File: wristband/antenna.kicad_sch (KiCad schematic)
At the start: 1 part

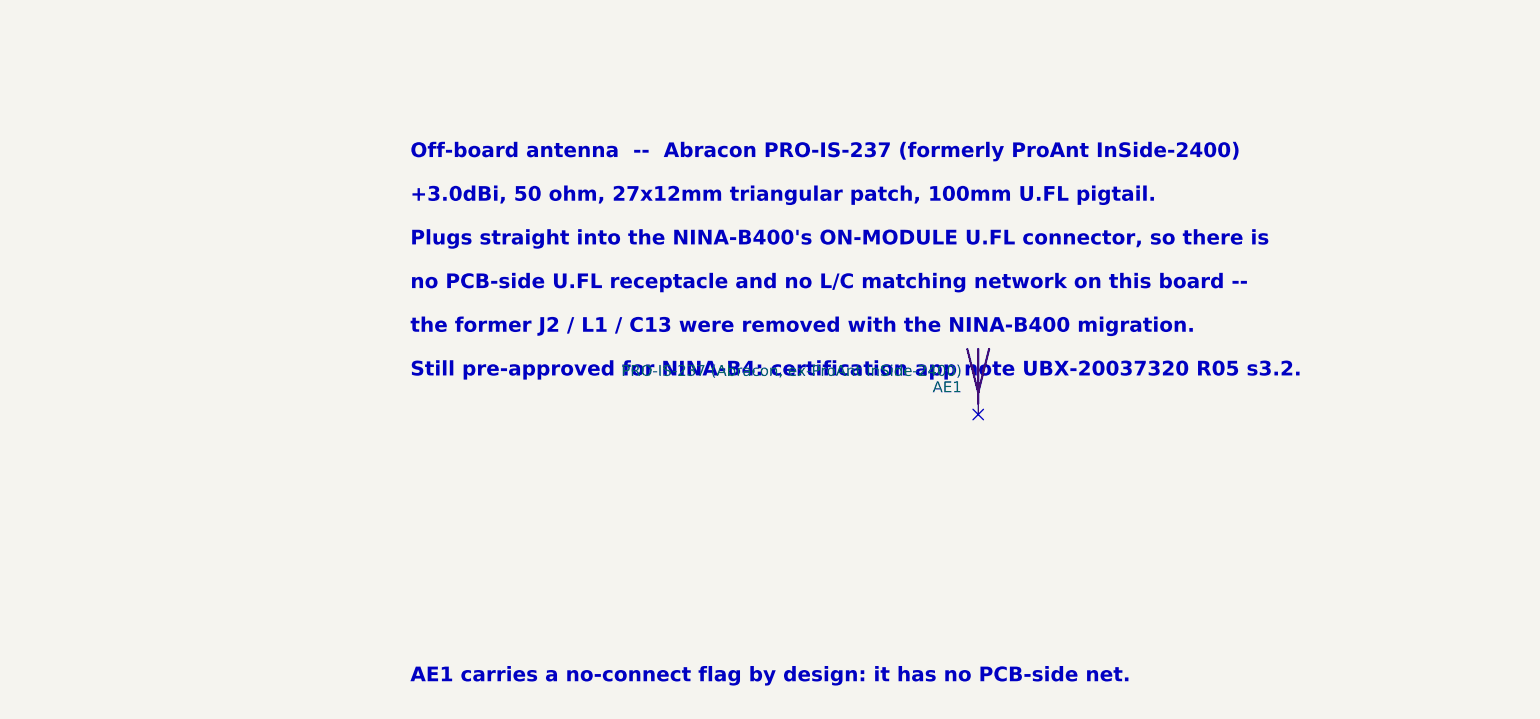
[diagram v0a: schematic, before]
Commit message: Convert global labels to power symbols; import footprints to PCB
Continues the ground cleanup from 0263e7f across the rest of the wristband
sheets: global labels replaced with explicit power symbols and wired
junctions, so connections are drawn rather than implied by name.

                     wires      labels      junctions   symbols
  power_bms          61 -> 83   61 -> 51    0 -> 3      25 -> 36
  programming_debug   7 ->  8    7 ->  4    0 -> 1       1 ->  3
  radio_mcu          71 -> 79   64 -> 42    7 -> 17     18 -> 32
  regulation          7 ->  7    7 ->  4    0 -> 0       3 ->  6

The added symbols are all power ports, so the BOM is untouched: still 47
components, 76 nets, 42 no-connects, 35 analyzer findings with 1 error --
identical before and after. The one error is the known DW01A false
positive (U1.6 GND sits on CELL_N by design, per the reference circuit).

Also ran Update PCB from Schematic on the wristband: 0 -> 46 footprints.
Nothing routed yet, no zones, board outline unchanged.

Co-Authored-By: Claude Opus 5 (1M context) <noreply@anthropic.com>
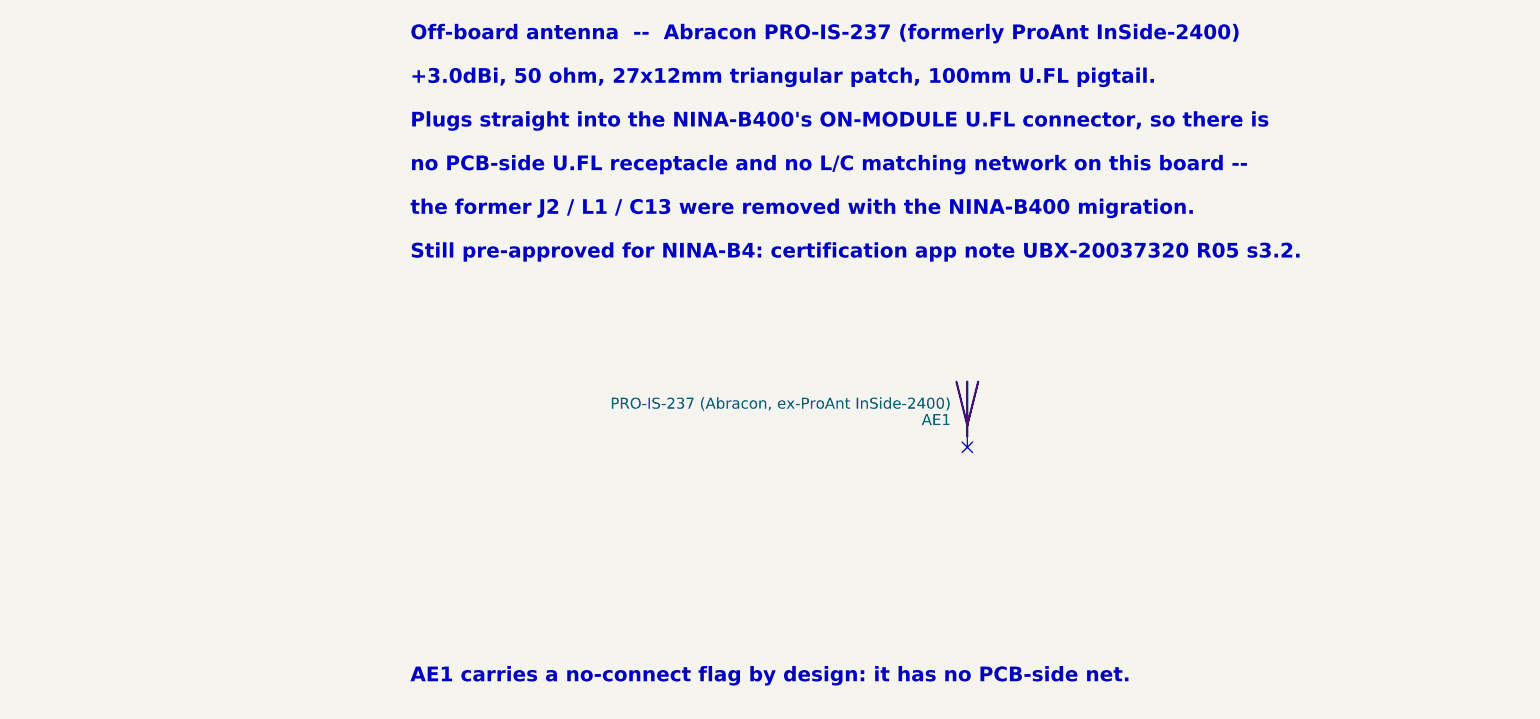
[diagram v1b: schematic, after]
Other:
- moved on the sheet: AE1
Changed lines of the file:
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@@
 	(text "Still pre-approved for NINA-B4: certification app note UBX-20037320 R05 s3.2."
 		(exclude_from_sim no)
-		(at 76.2 76.2 0)
+		(at 76.2 62.484 0)
 		(effects
 			(font
@@
 	(text "Off-board antenna  --  Abracon PRO-IS-237 (formerly ProAnt InSide-2400)"
 		(exclude_from_sim no)
-		(at 76.2 50.8 0)
+		(at 76.2 37.084 0)
 		(effects
 			(font
@@
 	(text "no PCB-side U.FL receptacle and no L/C matching network on this board --"
 		(exclude_from_sim no)
-		(at 76.2 66.04 0)
+		(at 76.2 52.324 0)
 		(effects
 			(font
@@
 	(text "+3.0dBi, 50 ohm, 27x12mm triangular patch, 100mm U.FL pigtail."
 		(exclude_from_sim no)
-		(at 76.2 55.88 0)
+		(at 76.2 42.164 0)
 		(effects
 			(font
@@
 	(text "the former J2 / L1 / C13 were removed with the NINA-B400 migration."
 		(exclude_from_sim no)
-		(at 76.2 71.12 0)
+		(at 76.2 57.404 0)
 		(effects
 			(font
@@
 	(text "Plugs straight into the NINA-B400's ON-MODULE U.FL connector, so there is"
 		(exclude_from_sim no)
-		(at 76.2 60.96 0)
+		(at 76.2 47.244 0)
 		(effects
 			(font
@@
 	)
 	(no_connect
-		(at 142.24 81.28)
+		(at 140.97 85.09)
 	)
 	(symbol
 		(lib_id "Device:Antenna")
-		(at 142.24 76.2 0)
+		(at 140.97 80.01 0)
 		(unit 1)
 		(body_style 1)
@@
 		(dnp no)
 		(property "Reference" "AE1"
-			(at 140.335 78.105 0)
+			(at 139.065 81.915 0)
 			(show_name no)
 			(do_not_autoplace no)
@@
 		)
 		(property "Value" "PRO-IS-237 (Abracon, ex-ProAnt InSide-2400)"
-			(at 140.335 76.2 0)
+			(at 139.065 80.01 0)
 			(show_name no)
 			(do_not_autoplace no)
@@
 		)
 		(property "Footprint" ""
-			(at 142.24 76.2 0)
+			(at 140.97 80.01 0)
 			(hide yes)
 			(show_name no)
@@
 		)
 		(property "Datasheet" ""
-			(at 142.24 76.2 0)
+			(at 140.97 80.01 0)
 			(hide yes)
 			(show_name no)
@@
 		)
 		(property "Description" ""
-			(at 142.24 76.2 0)
+			(at 140.97 80.01 0)
 			(show_name no)
 			(do_not_autoplace no)
@@
 		)
 		(property "MPN" "PRO-IS-237"
-			(at 140.335 78.105 0)
+			(at 139.065 81.915 0)
 			(hide yes)
 			(show_name no)
@@
 		)
 		(property "Manufacturer" "Abracon"
-			(at 140.335 78.105 0)
+			(at 139.065 81.915 0)
 			(hide yes)
 			(show_name no)

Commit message: Migrate wristband to DWM3001C; swap LDO to TPS7A02; fix ERC
Replace the NINA-B400 + DWM3000 pair with a single Qorvo DWM3001C, then
replace the MCP1700 LDO with a nanopower TI TPS7A0233. Wristband ERC goes
from 1 error / 13 warnings to 0 errors / 1 warning.

DWM3001C (U4), verified against Qorvo DS Rev B May 2022:
- Integrates DW3110 UWB + nRF52833 BLE MCU + LIS2DH12 + UWB antenna +
  Bluetooth chip antenna + 38.4MHz crystal. Its nRF52833 is now the host,
  so U3 (NINA-B400) is deleted.
- The DW3110<->nRF52833 SPI is internal, so the board-level UWB SPI bus,
  IRQ/RSTn/WAKEUP, the GPIO5/6 SPI-mode straps (R7/R8), the IRQ pulldown
  (R9) and the external LFXO (Y1/C14/C15) are all gone. C8-C10 too.
- AE1 (PRO-IS-237) removed: the module carries both antennas, so
  antenna.kicad_sch is documentation-only and places nothing.
- SWD moved for the first time: SWD_CLK=2, SWD_DIO=3, RESET=47 (P0.18),
  SWO=28 (P1.00). Battery sense moved to P0.02 = AIN0. Both P1.00=SWO and
  P0.02=AIN0 confirmed in nRF52833 PS v1.7 p825-826.
- Symbol + DWM3001C_PLACEHOLDER footprint are wristband-only, in libs/.
  The footprint has TWO unresolved dimensions (side pitch back-derives to
  1.06375mm; bottom pad row width undimensioned and apparently off-centre).
  VERIFY BEFORE FAB.

TPS7A0233PDBVR (U5), verified against TI SBVS277C:
- Iq 1.6uA typ / 4uA max -> 25nA typ / 46nA max; it was the largest single
  standby draw, bigger than the DWM3001C's own 850nA sleep. Board standby
  ~4.3uA -> ~2.7uA. Accuracy +/-1.5% vs +/-2.5%.
- Not a drop-in: SOT-23-5 1=IN 2=GND 3=EN 4=NC 5=OUT. EN ties to VBAT
  because TPS7A02 is disabled when EN floats and the MCU on this rail
  cannot enable its own supply.
- C12 1uF -> 2.2uF for the 0.5uF effective-capacitance stability floor.
- Symbol is self-contained: KiCad ships no TPS7A02, and every TPS7A05
  sibling is extends-based, which kicad-cli cannot load.

ERC fixes:
- Real bug: regulation.kicad_sch had no labels at all, so U5's input and
  C11 sat on an iso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
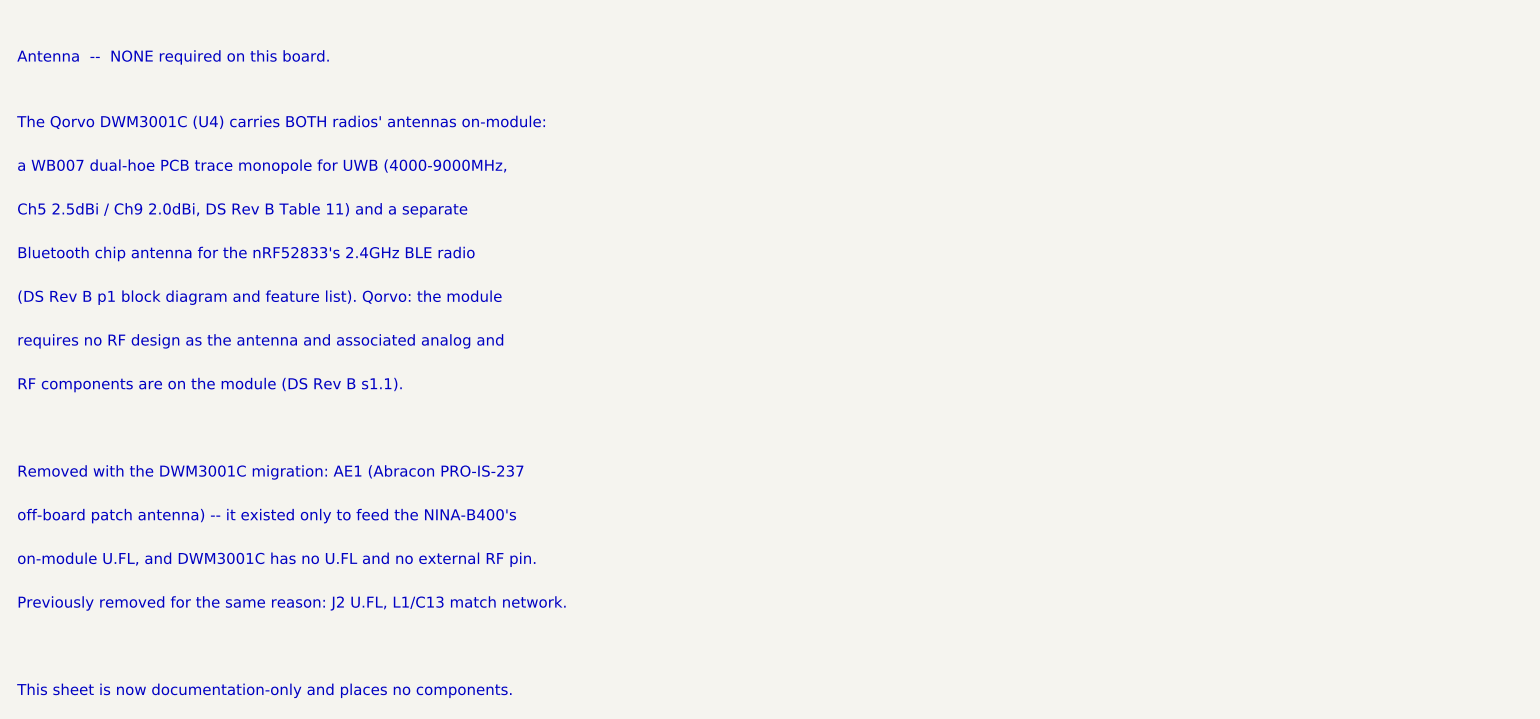
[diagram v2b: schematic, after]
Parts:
- removed AE1: PRO-IS-237 (Abracon, ex-ProAnt InSide-2400), symbol Device:Antenna
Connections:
- no-connect marks 1 -> 0
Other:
- note added: "(DS Rev B p1 block diagram and feature list). Qorvo: the module"
- note added: "Antenna -- NONE required on this board."
- note added: "Bluetooth chip antenna for the nRF52833's 2.4GHz BLE radio"
- note added: "Ch5 2.5dBi / Ch9 2.0dBi, DS Rev B Table 11) and a separate"
- note added: "Previously removed for the same reason: J2 U.FL, L1/C13 match network."
- note added: "RF components are on the module (DS Rev B s1.1)."
- note added: "Removed with the DWM3001C migration: AE1 (Abracon PRO-IS-237"
- note added: "The Qorvo DWM3001C (U4) carries BOTH radios' antennas on-module:"
- note added: "This sheet is now documentation-only and places no components."
- note added: "a WB007 dual-hoe PCB trace monopole for UWB (4000-9000MHz,"
- note added: "off-board patch antenna) -- it existed only to feed the NINA-B400's"
- note added: "on-module U.FL, and DWM3001C has no U.FL and no external RF pin."
- note added: "requires no RF design as the antenna and associated analog and"
- note removed: "+3.0dBi, 50 ohm, 27x12mm triangular patch, 100mm U.FL pigtail."
- note removed: "AE1 carries a no-connect flag by design: it has no PCB-side net."
- note removed: "Off-board antenna -- Abracon PRO-IS-237 (formerly ProAnt InSide-2400)"
- note removed: "Plugs straight into the NINA-B400's ON-MODULE U.FL connector, so there is"
- note removed: "Still pre-approved for NINA-B4: certification app note UBX-20037320 R05 s3.2."
- note removed: "no PCB-side U.FL receptacle and no L/C matching network on this board --"
- note removed: "the former J2 / L1 / C13 were removed with the NINA-B400 migration."
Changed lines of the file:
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@@
 		(comment 1 "Wristband NINA-B400 external antenna -- plugs into the module's ON-BOARD U.FL connector; no PCB-side U.FL or L/C match network needed")
 	)
-	(text "AE1 carries a no-connect flag by design: it has no PCB-side net."
+	(text "Antenna  --  NONE required on this board."
 		(exclude_from_sim no)
-		(at 76.2 111.76 0)
+		(at 30.48 40.64 0)
 		(effects
 			(font
-				(size 1.7 1.7)
-				(bold yes)
+				(size 1.27 1.27)
 			)
-			(justify left)
+			(justify left bottom)
 		)
 	)
-	(text "Still pre-approved for NINA-B4: certification app note UBX-20037320 R05 s3.2."
+	(text "The Qorvo DWM3001C (U4) carries BOTH radios' antennas on-module:"
 		(exclude_from_sim no)
-		(at 76.2 62.484 0)
+		(at 30.48 48.26 0)
 		(effects
 			(font
-				(size 1.7 1.7)
-				(bold yes)
+				(size 1.27 1.27)
 			)
-			(justify left)
+			(justify left bottom)
 		)
 	)
-	(text "Off-board antenna  --  Abracon PRO-IS-237 (formerly ProAnt InSide-2400)"
+	(text "a WB007 dual-hoe PCB trace monopole for UWB (4000-9000MHz,"
 		(exclude_from_sim no)
-		(at 76.2 37.084 0)
+		(at 30.48 53.34 0)
 		(effects
 			(font
-				(size 1.7 1.7)
-				(bold yes)
+				(size 1.27 1.27)
 			)
-			(justify left)
+			(justify left bottom)
 		)
 	)
-	(text "no PCB-side U.FL receptacle and no L/C matching network on this board --"
+	(text "Ch5 2.5dBi / Ch9 2.0dBi, DS Rev B Table 11) and a separate"
 		(exclude_from_sim no)
-		(at 76.2 52.324 0)
+		(at 30.48 58.42 0)
 		(effects
 			(font
-				(size 1.7 1.7)
-				(bold yes)
+				(size 1.27 1.27)
 			)
-			(justify left)
+			(justify left bottom)
 		)
 	)
-	(text "+3.0dBi, 50 ohm, 27x12mm triangular patch, 100mm U.FL pigtail."
+	(text "Bluetooth chip antenna for the nRF52833's 2.4GHz BLE radio"
 		(exclude_from_sim no)
-		(at 76.2 42.164 0)
+		(at 30.48 63.5 0)
 		(effects
 			(font
-				(size 1.7 1.7)
-				(bold yes)
+				(size 1.27 1.27)
 			)
-			(justify left)
+			(justify left bottom)
 		)
 	)
-	(text "the former J2 / L1 / C13 were removed with the NINA-B400 migration."
+	(text "(DS Rev B p1 block diagram and feature list). Qorvo: the module"
 		(exclude_from_sim no)
-		(at 76.2 57.404 0)
+		(at 30.48 68.58 0)
 		(effects
 			(font
-				(size 1.7 1.7)
-				(bold yes)
+				(size 1.27 1.27)
 			)
-			(justify left)
+			(justify left bottom)
 		)
 	)
-	(text "Plugs straight into the NINA-B400's ON-MODULE U.FL connector, so there is"
+	(text "requires no RF design as the antenna and associated analog and"
 		(exclude_from_sim no)
-		(at 76.2 47.244 0)
+		(at 30.48 73.66 0)
 		(effects
 			(font
-				(size 1.7 1.7)
-				(bold yes)
+				(size 1.27 1.27)
 			)
-			(justify left)
+			(justify left bottom)
 		)
 	)
-	(no_connect
-		(at 140.97 85.09)
-	)
-	(symbol
-		(lib_id "Device:Antenna")
-		(at 140.97 80.01 0)
-		(unit 1)
-		(body_style 1)
+	(text "RF components are on the module (DS Rev B s1.1)."
 		(exclude_from_sim no)
-		(in_bom yes)
-		(on_board yes)
-		(in_pos_files yes)
-		(dnp no)
-		(property "Reference" "AE1"
-			(at 139.065 81.915 0)
-			(show_name no)
-			(do_not_autoplace no)
-			(effects
-				(font
-					(size 1.27 1.27)
-				)
-				(justify right)
+		(at 30.48 78.74 0)
+		(effects
+			(font
+				(size 1.27 1.27)
 			)
-		)
-		(property "Value" "PRO-IS-237 (Abracon, ex-ProAnt InSide-2400)"
-			(at 139.065 80.01 0)
-			(show_name no)
-			(do_not_autoplace no)
-			(effects
-				(font
-					(size 1.27 1.27)
-				)
-				(justify right)
-			)
-		)
-		(property "Footprint" ""
-			(at 140.97 80.01 0)
-			(hide yes)
-			(show_name no)
-			(do_not_autoplace no)
-			(effects
-				(font
-					(size 1.27 1.27)
-				)
-			)
-		)
-		(property "Datasheet" ""
-			(at 140.97 80.01 0)
-			(hide yes)
-			(show_name no)
-			(do_not_autoplace no)
-			(effects
-				(font
-					(size 1.27 1.27)
-				)
-			)
-		)
-		(property "Description" ""
-			(at 140.97 80.01 0)
-			(show_name no)
-			(do_not_autoplace no)
-			(effects
-				(font
-					(size 1.27 1.27)
-				)
-			)
-		)
-		(property "MPN" "PRO-IS-237"
-			(at 139.065 81.915 0)
-			(hide yes)
-			(show_name no)
-			(do_not_autoplace no)
-			(effects
-				(font
-					(size 1.27 1.27)
-				)
-			)
-		)
-		(property "Manufacturer" "Abracon"
-			(at 139.065 81.915 0)
-			(hide yes)
-			(show_name no)
-			(do_not_autoplace no)
-			(effects
-				(font
-					(size 1.27 1.27)
-				)
-			)
-		)
-		(pin "1"
-		)
-		(instances
-			(project "wristband"
-				(path "/b3417696-fb19-4c3e-bd30-28bb2d157bef/70531719-0575-447f-9fe2-78b3cc25b488"
-					(reference "AE1")
-					(unit 1)
-				)
-			)
+			(justify left bottom)
 		)
 	)
+	(text "Removed with the DWM3001C migration: AE1 (Abracon PRO-IS-237"
+		(exclude_from_sim no)
+		(at 30.48 88.9 0)
+		(effects
+			(font
+				(size 1.27 1.27)
+			)
+			(justify left bottom)
+		)
+	)
+	(text "off-board patch antenna) -- it existed only to feed the NINA-B400's"
+		(exclude_from_sim no)
+		(at 30.48 93.98 0)
+		(effects
+			(font
+				(size 1.27 1.27)
+			)
+			(justify left bottom)
+		)
+	)
+	(text "on-module U.FL, and DWM3001C has no U.FL and no external RF pin."
+		(exclude_from_sim no)
+		(at 30.48 99.06 0)
+		(effects
+			(font
+				(size 1.27 1.27)
+			)
+			(justify left bottom)
+		)
+	)
+	(text "Previously removed for the same reason: J2 U.FL, L1/C13 match network."
+		(exclude_from_sim no)
+		(at 30.48 104.14 0)
+		(effects
+			(font
+				(size 1.27 1.27)
+			)
+			(justify left bottom)
+		)
+	)
+	(text "This sheet is now documentation-only and places no components."
+		(exclude_from_sim no)
+		(at 30.48 114.3 0)
+		(effects
+			(font
+				(size 1.27 1.27)
+			)
+			(justify left bottom)
+		)
+	)
